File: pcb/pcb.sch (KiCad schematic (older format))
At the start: 22 parts, among them J1 VIN VBAT, J2 Conn_01x04, J3 AudioJack3, J4 Conn_01x04, J5 HX711, J6 Conn_01x04, J7 Conn_01x04, J8 Conn_01x08, SW1 SW_DPDT_x2, U1 LM386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

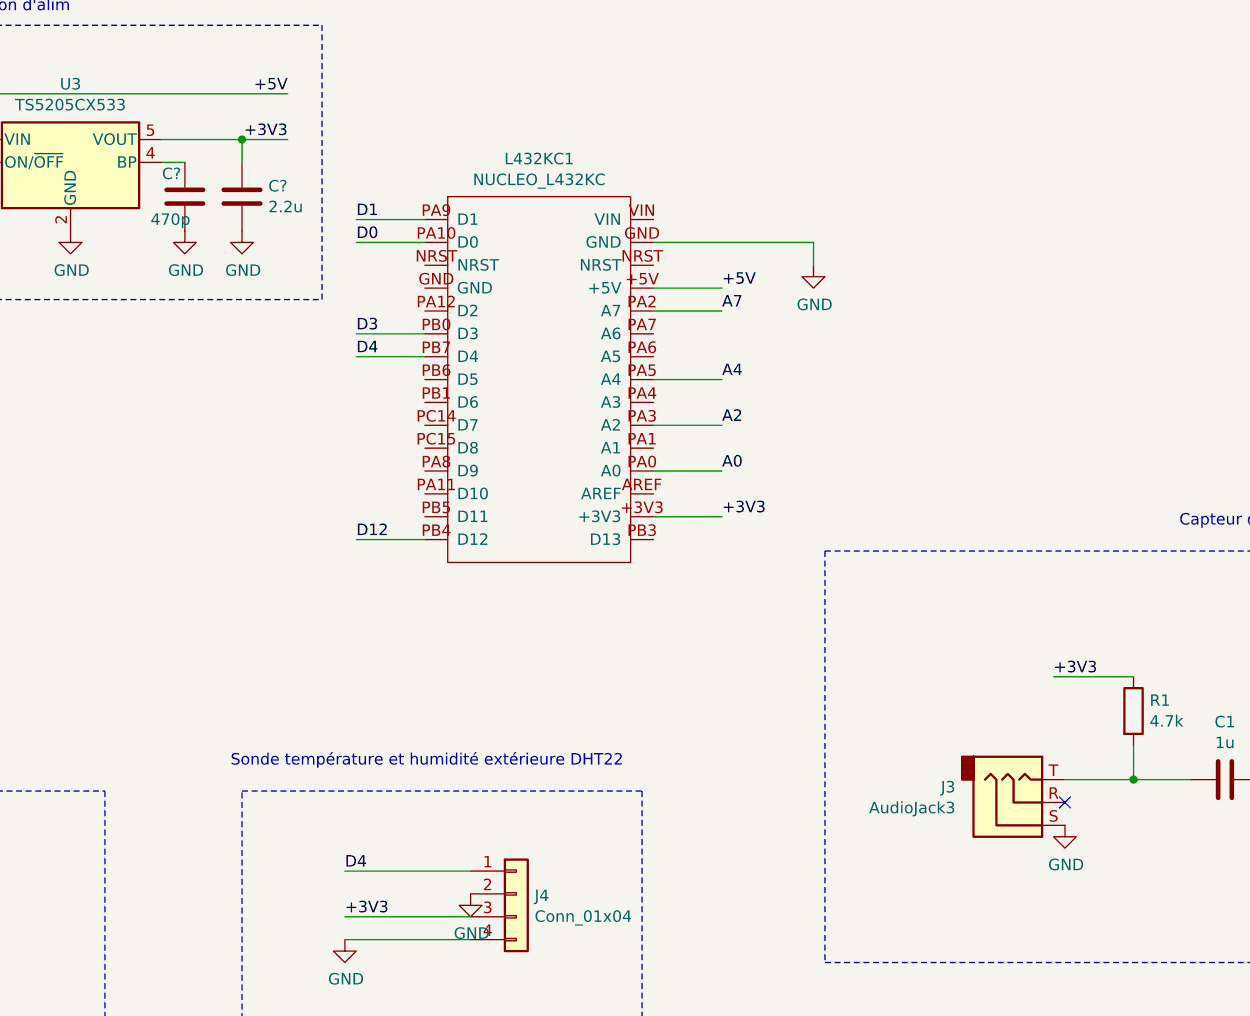
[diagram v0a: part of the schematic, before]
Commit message: Audio jack a la masse
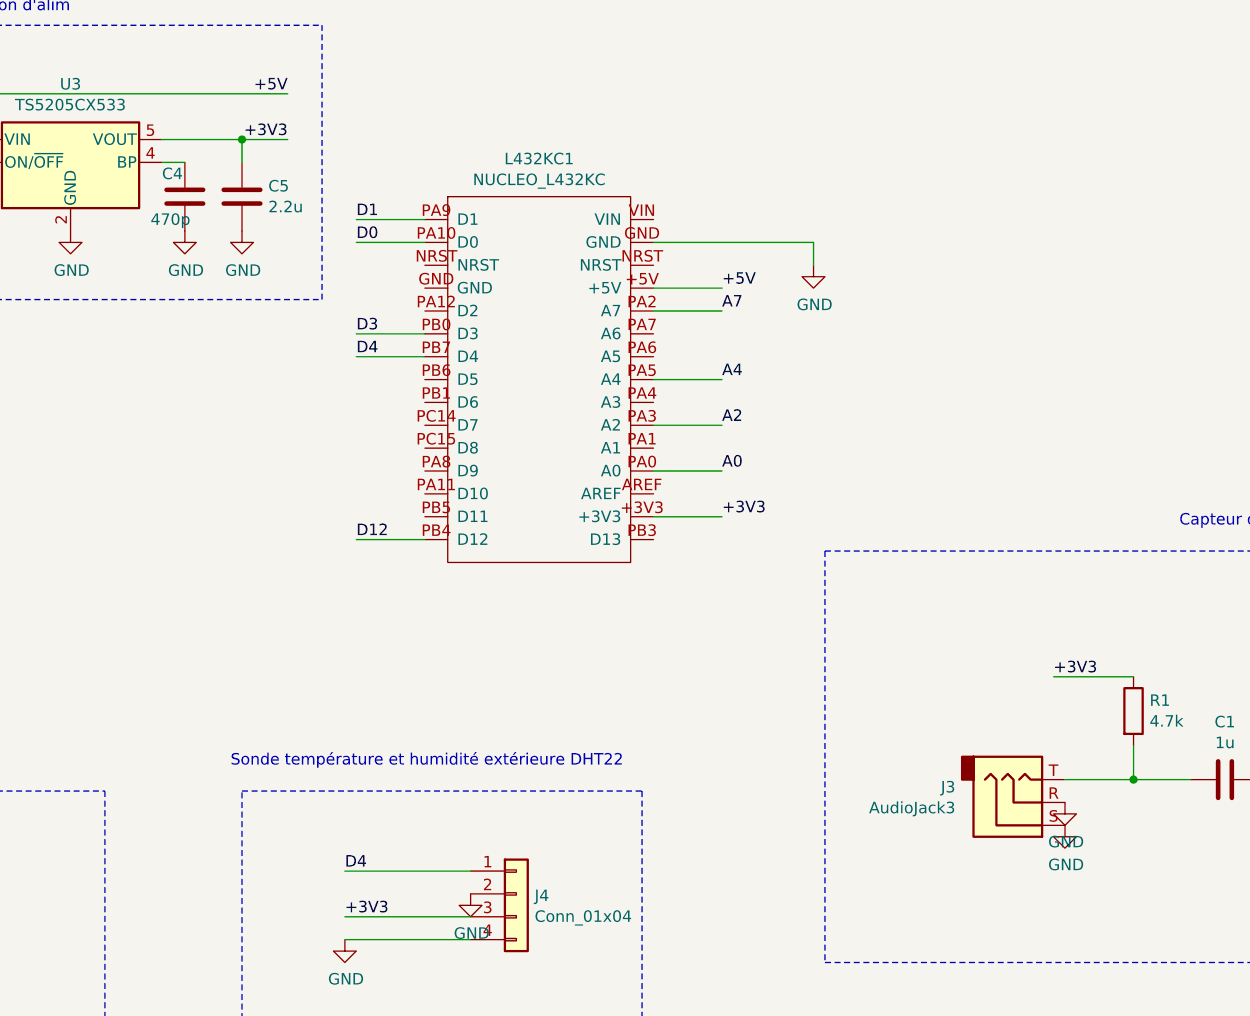
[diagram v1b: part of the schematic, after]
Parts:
- C4, C5: renamed from C?; footprint (none) -> Capacitor_SMD:C_0805_2012Metric_Pad1.18x1.45mm_HandSolder
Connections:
- net GND: now also J3.R
- no-connect marks 3 -> 2
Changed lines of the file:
@@
 	1    0    0    -1
 $EndComp
-NoConn ~ 8150 5650
 Wire Wire Line
 	8150 5550 8450 5550
@@
 $EndComp
 $Comp
-L Device:C C?
+L Device:C C4
 U 1 1 5FBFE6BC
 P 4300 3000
-F 0 "C?" H 4200 3100 50  0000 L CNN
+F 0 "C4" H 4200 3100 50  0000 L CNN
 F 1 "470p" H 4150 2900 50  0000 L CNN
-F 2 "" H 4338 2850 50  0001 C CNN
+F 2 "Capacitor_SMD:C_0805_2012Metric_Pad1.18x1.45mm_HandSolder" H 4338 2850 50  0001 C CNN
 F 3 "~" H 4300 3000 50  0001 C CNN
 	1    4300 3000
@@
 $EndComp
 $Comp
-L power:GND #PWR?
+L power:GND #PWR0122
 U 1 1 5FBFF114
 P 4300 3150
-F 0 "#PWR?" H 4300 2900 50  0001 C CNN
+F 0 "#PWR0122" H 4300 2900 50  0001 C CNN
 F 1 "GND" H 4305 2977 50  0000 C CNN
 F 2 "" H 4300 3150 50  0001 C CNN
@@
 	4300 2850 4200 2850
 $Comp
-L Device:C C?
+L Device:C C5
 U 1 1 5FC01AAB
 P 4550 3000
-F 0 "C?" H 4665 3046 50  0000 L CNN
+F 0 "C5" H 4665 3046 50  0000 L CNN
 F 1 "2.2u" H 4665 2955 50  0000 L CNN
-F 2 "" H 4588 2850 50  0001 C CNN
+F 2 "Capacitor_SMD:C_0805_2012Metric_Pad1.18x1.45mm_HandSolder" H 4588 2850 50  0001 C CNN
 F 3 "~" H 4550 3000 50  0001 C CNN
 	1    4550 3000
@@
 	4200 2750 4550 2750
 $Comp
-L power:GND #PWR?
+L power:GND #PWR0123
 U 1 1 5FC05656
 P 4550 3150
-F 0 "#PWR?" H 4550 2900 50  0001 C CNN
+F 0 "#PWR0123" H 4550 2900 50  0001 C CNN
 F 1 "GND" H 4555 2977 50  0000 C CNN
 F 2 "" H 4550 3150 50  0001 C CNN
@@
 Text Label 4750 2550 2    50   ~ 0
 +5V
+$Comp
+L power:GND #PWR?
+U 1 1 5FBD517C
+P 8150 5650
+F 0 "#PWR?" H 8150 5400 50  0001 C CNN
+F 1 "GND" H 8155 5477 50  0000 C CNN
+F 2 "" H 8150 5650 50  0001 C CNN
+F 3 "" H 8150 5650 50  0001 C CNN
+	1    8150 5650
+	1    0    0    -1
+$EndComp
 $EndSCHEMATC

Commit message: Modification empreintes
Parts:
- C1: footprint Capacitor_THT:CP_Radial_D5.0mm_P2.00mm -> Capacitor_THT:CP_Radial_D6.3mm_P2.50mm
- C3: footprint Capacitor_THT:CP_Radial_D4.0mm_P1.50mm -> Capacitor_THT:CP_Radial_D6.3mm_P2.50mm
- J5: footprint Connector_PinHeader_2.00mm:PinHeader_1x04_P2.00mm_Vertical -> Connector_PinHeader_2.54mm:PinHeader_1x04_P2.54mm_Vertical
- J8: footprint Connector_PinHeader_2.00mm:PinHeader_1x08_P2.00mm_Vertical -> Connector_PinHeader_2.54mm:PinHeader_1x08_P2.54mm_Vertical
- R1, R2, R3: footprint Resistor_THT:R_Axial_DIN0204_L3.6mm_D1.6mm_P5.08mm_Horizontal -> Resistor_THT:R_Axial_DIN0207_L6.3mm_D2.5mm_P10.16mm_Horizontal
- R4, R5: footprint Resistor_THT:R_Axial_DIN0204_L3.6mm_D1.6mm_P5.08mm_Vertical -> Resistor_THT:R_Axial_DIN0207_L6.3mm_D2.5mm_P10.16mm_Horizontal
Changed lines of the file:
@@
 F 0 "J5" H 6380 1242 50  0000 L CNN
 F 1 "HX711" H 6380 1151 50  0000 L CNN
-F 2 "Connector_PinHeader_2.00mm:PinHeader_1x04_P2.00mm_Vertical" H 6300 1250 50  0001 C CNN
+F 2 "Connector_PinHeader_2.54mm:PinHeader_1x04_P2.54mm_Vertical" H 6300 1250 50  0001 C CNN
 F 3 "~" H 6300 1250 50  0001 C CNN
 	1    6300 1250
@@
 F 0 "R1" H 8520 5296 50  0000 L CNN
 F 1 "4.7k" H 8520 5205 50  0000 L CNN
-F 2 "Resistor_THT:R_Axial_DIN0204_L3.6mm_D1.6mm_P5.08mm_Horizontal" V 8380 5250 50  0001 C CNN
+F 2 "Resistor_THT:R_Axial_DIN0207_L6.3mm_D2.5mm_P10.16mm_Horizontal" V 8380 5250 50  0001 C CNN
 F 3 "~" H 8450 5250 50  0001 C CNN
 	1    8450 5250
@@
 F 0 "C1" V 8598 5550 50  0000 C CNN
 F 1 "1u" V 8689 5550 50  0000 C CNN
-F 2 "Capacitor_THT:CP_Radial_D5.0mm_P2.00mm" H 8888 5400 50  0001 C CNN
+F 2 "Capacitor_THT:CP_Radial_D6.3mm_P2.50mm" H 8888 5400 50  0001 C CNN
 F 3 "~" H 8850 5550 50  0001 C CNN
 	1    8850 5550
@@
 F 0 "C3" V 9698 5650 50  0000 C CNN
 F 1 "1u" V 9789 5650 50  0000 C CNN
-F 2 "Capacitor_THT:CP_Radial_D4.0mm_P1.50mm" H 9988 5500 50  0001 C CNN
+F 2 "Capacitor_THT:CP_Radial_D6.3mm_P2.50mm" H 9988 5500 50  0001 C CNN
 F 3 "~" H 9950 5650 50  0001 C CNN
 	1    9950 5650
@@
 F 0 "R2" H 10270 5346 50  0000 L CNN
 F 1 "10k" H 10270 5255 50  0000 L CNN
-F 2 "Resistor_THT:R_Axial_DIN0204_L3.6mm_D1.6mm_P5.08mm_Horizontal" V 10130 5300 50  0001 C CNN
+F 2 "Resistor_THT:R_Axial_DIN0207_L6.3mm_D2.5mm_P10.16mm_Horizontal" V 10130 5300 50  0001 C CNN
 F 3 "~" H 10200 5300 50  0001 C CNN
 	1    10200 5300
@@
 F 0 "R3" H 10270 5996 50  0000 L CNN
 F 1 "10k" H 10270 5905 50  0000 L CNN
-F 2 "Resistor_THT:R_Axial_DIN0204_L3.6mm_D1.6mm_P5.08mm_Horizontal" V 10130 5950 50  0001 C CNN
+F 2 "Resistor_THT:R_Axial_DIN0207_L6.3mm_D2.5mm_P10.16mm_Horizontal" V 10130 5950 50  0001 C CNN
 F 3 "~" H 10200 5950 50  0001 C CNN
 	1    10200 5950
@@
 F 0 "R4" H 1870 2146 50  0000 L CNN
 F 1 "1K" H 1870 2055 50  0000 L CNN
-F 2 "Resistor_THT:R_Axial_DIN0204_L3.6mm_D1.6mm_P5.08mm_Vertical" V 1730 2100 50  0001 C CNN
+F 2 "Resistor_THT:R_Axial_DIN0207_L6.3mm_D2.5mm_P10.16mm_Horizontal" V 1730 2100 50  0001 C CNN
 F 3 "~" H 1800 2100 50  0001 C CNN
 	1    1800 2100
@@
 F 0 "R5" H 1870 2446 50  0000 L CNN
 F 1 "2k" H 1870 2355 50  0000 L CNN
-F 2 "Resistor_THT:R_Axial_DIN0204_L3.6mm_D1.6mm_P5.08mm_Vertical" V 1730 2400 50  0001 C CNN
+F 2 "Resistor_THT:R_Axial_DIN0207_L6.3mm_D2.5mm_P10.16mm_Horizontal" V 1730 2400 50  0001 C CNN
 F 3 "~" H 1800 2400 50  0001 C CNN
 	1    1800 2400
@@
 F 0 "J8" H 1818 3825 50  0000 C CNN
 F 1 "Conn_01x08" H 1818 3916 50  0000 C CNN
-F 2 "Connector_PinHeader_2.00mm:PinHeader_1x08_P2.00mm_Vertical" H 1900 4450 50  0001 C CNN
+F 2 "Connector_PinHeader_2.54mm:PinHeader_1x08_P2.54mm_Vertical" H 1900 4450 50  0001 C CNN
 F 3 "~" H 1900 4450 50  0001 C CNN
 	1    1900 4450
@@
 +5V
 $Comp
-L power:GND #PWR?
+L power:GND #PWR0124
 U 1 1 5FBD517C
 P 8150 5650
-F 0 "#PWR?" H 8150 5400 50  0001 C CNN
+F 0 "#PWR0124" H 8150 5400 50  0001 C CNN
 F 1 "GND" H 8155 5477 50  0000 C CNN
 F 2 "" H 8150 5650 50  0001 C CNN

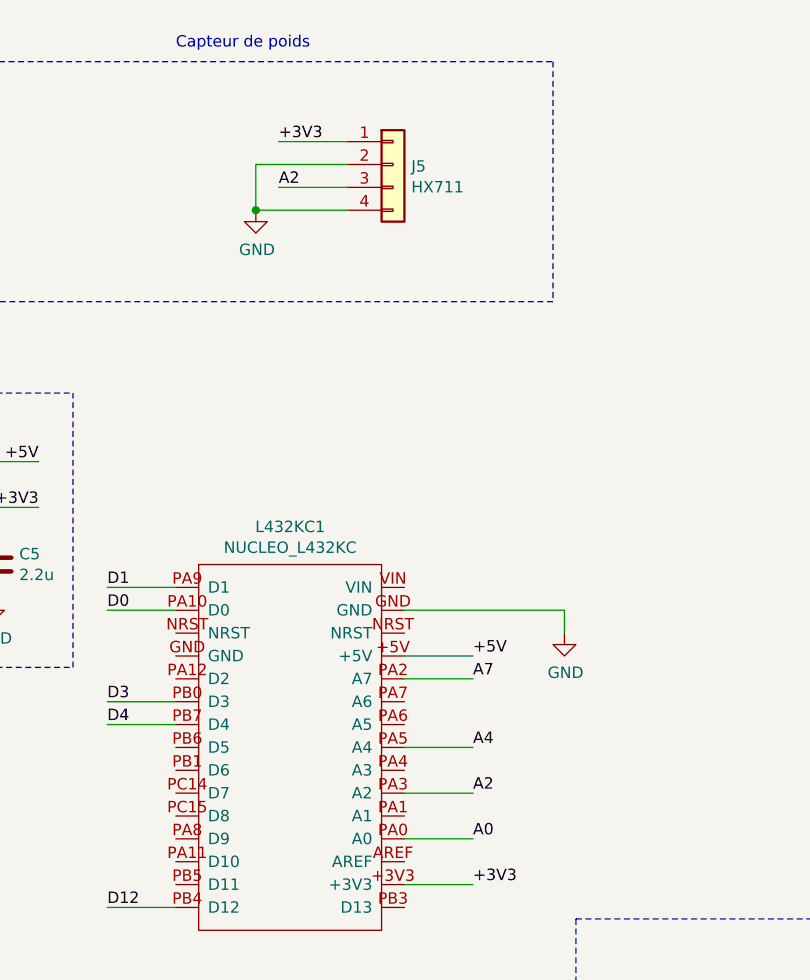
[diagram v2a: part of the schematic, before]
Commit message: Modification pin HX711
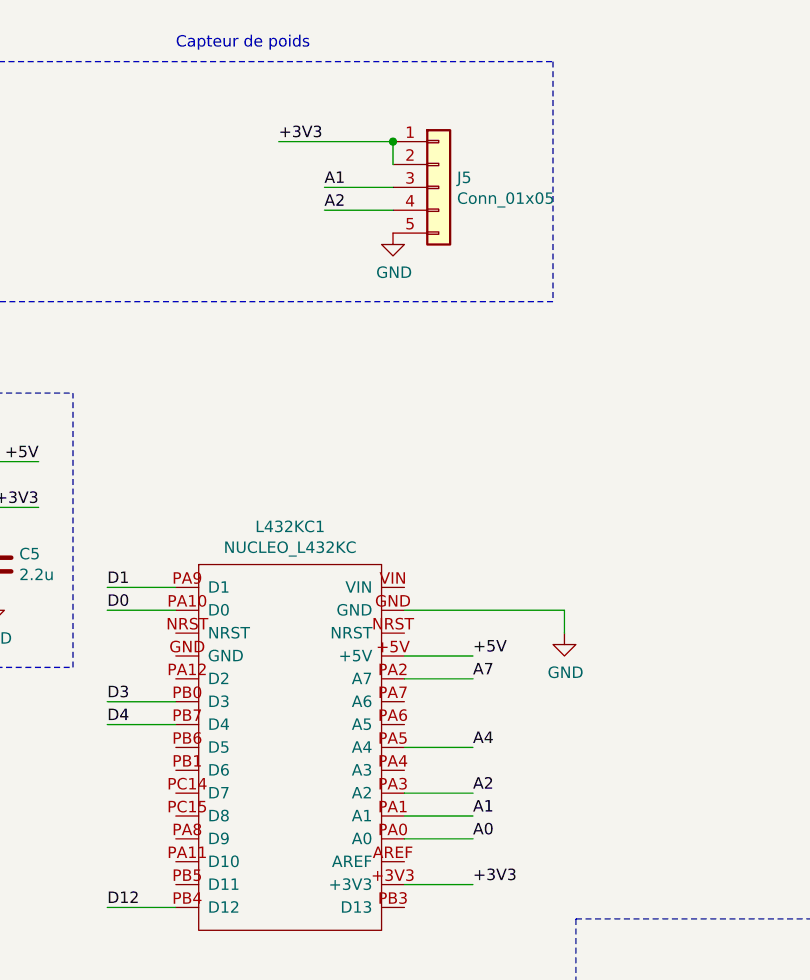
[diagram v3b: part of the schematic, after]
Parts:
- removed J5: HX711, Connector_PinHeader_2.54mm:PinHeader_1x04_P2.54mm_Vertical, symbol Connector_Generic:Conn_01x04
- added J5: Conn_01x05, Connector_PinHeader_2.54mm:PinHeader_1x05_P2.54mm_Vertical, symbol Connector_Generic:Conn_01x05
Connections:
- net +3V3: now also J5.1 (Pin_1), J5.2 (Pin_2)
- net A2: now also J5.4 (Pin_4)
- net GND: now also J5.5 (Pin_5)
- net A1: now reaches L432KC1.PA1 (A1)
- net A1: now also J5.3 (Pin_3)
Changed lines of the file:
@@
 Text Notes 5350 750  0    50   ~ 0
 Capteur de poids
-$Comp
-L Connector_Generic:Conn_01x04 J5
-U 1 1 5FB2C9F7
-P 6300 1250
-F 0 "J5" H 6380 1242 50  0000 L CNN
-F 1 "HX711" H 6380 1151 50  0000 L CNN
-F 2 "Connector_PinHeader_2.54mm:PinHeader_1x04_P2.54mm_Vertical" H 6300 1250 50  0001 C CNN
-F 3 "~" H 6300 1250 50  0001 C CNN
-	1    6300 1250
-	1    0    0    -1
-$EndComp
-Wire Wire Line
-	6100 1150 5800 1150
-Wire Wire Line
-	6100 1350 5800 1350
+Wire Wire Line
+	6300 1350 6000 1350
 Text Label 5800 1150 0    50   ~ 0
 +3V3
-Text Label 5800 1350 0    50   ~ 0
-A2
-Wire Wire Line
-	5700 1250 5700 1450
-Wire Wire Line
-	5700 1250 6100 1250
-Wire Wire Line
-	5700 1450 6100 1450
-$Comp
-L power:GND #PWR0102
-U 1 1 5FB34119
-P 5700 1450
-F 0 "#PWR0102" H 5700 1200 50  0001 C CNN
-F 1 "GND" H 5705 1277 50  0000 C CNN
-F 2 "" H 5700 1450 50  0001 C CNN
-F 3 "" H 5700 1450 50  0001 C CNN
-	1    5700 1450
-	1    0    0    -1
-$EndComp
-Connection ~ 5700 1450
 Wire Wire Line
 	6350 4000 6650 4000
@@
 	1    0    0    -1
 $EndComp
+$Comp
+L Connector_Generic:Conn_01x05 J5
+U 1 1 5FCC2112
+P 6500 1350
+F 0 "J5" H 6580 1392 50  0000 L CNN
+F 1 "Conn_01x05" H 6580 1301 50  0000 L CNN
+F 2 "Connector_PinHeader_2.54mm:PinHeader_1x05_P2.54mm_Vertical" H 6500 1350 50  0001 C CNN
+F 3 "~" H 6500 1350 50  0001 C CNN
+	1    6500 1350
+	1    0    0    -1
+$EndComp
+Wire Wire Line
+	5800 1150 6300 1150
+Wire Wire Line
+	6300 1450 6000 1450
+$Comp
+L power:GND #PWR0102
+U 1 1 5FCCD986
+P 6300 1550
+F 0 "#PWR0102" H 6300 1300 50  0001 C CNN
+F 1 "GND" H 6305 1377 50  0000 C CNN
+F 2 "" H 6300 1550 50  0001 C CNN
+F 3 "" H 6300 1550 50  0001 C CNN
+	1    6300 1550
+	1    0    0    -1
+$EndComp
+Wire Wire Line
+	6300 1250 6300 1150
+Connection ~ 6300 1150
+Wire Wire Line
+	6350 4100 6650 4100
+Text Label 6650 4100 0    50   ~ 0
+A1
+Text Label 6000 1350 0    50   ~ 0
+A1
+Text Label 6000 1450 0    50   ~ 0
+A2
 $EndSCHEMATC

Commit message: Ajout via
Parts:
- R4: value 1K -> 2.2k
- R5: value 2k -> 3.3k
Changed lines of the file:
@@
 P 1800 2100
 F 0 "R4" H 1870 2146 50  0000 L CNN
-F 1 "1K" H 1870 2055 50  0000 L CNN
+F 1 "2.2k" H 1870 2055 50  0000 L CNN
 F 2 "Resistor_THT:R_Axial_DIN0207_L6.3mm_D2.5mm_P10.16mm_Horizontal" V 1730 2100 50  0001 C CNN
 F 3 "~" H 1800 2100 50  0001 C CNN
@@
 P 1800 2400
 F 0 "R5" H 1870 2446 50  0000 L CNN
-F 1 "2k" H 1870 2355 50  0000 L CNN
+F 1 "3.3k" H 1870 2355 50  0000 L CNN
 F 2 "Resistor_THT:R_Axial_DIN0207_L6.3mm_D2.5mm_P10.16mm_Horizontal" V 1730 2400 50  0001 C CNN
 F 3 "~" H 1800 2400 50  0001 C CNN
